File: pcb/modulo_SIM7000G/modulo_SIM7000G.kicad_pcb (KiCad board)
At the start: 2 copper layers, 100 x 50 mm, 56 parts, among them J1 Conn_01x04, J2 115Q-BCA0, J3 CONECTOR SERIAL, J4 Conn_01x02, J5 DCJ200-10-A-XX-X_REVA, Q1 NTE4153NT1G, Q2 NTE4153NT1G, Q3 NTE4153NT1G, U1 SIM7000G, U2 SN74LV1T34DCKR, U3 SN74LV1T34DCKR, U4 SN74LV1T34DCKR, U5 SN74LV1T34DCKR, U6 SN74LV1T34DCKR, U7 MIC29302WU, U8 LM1117-3.3

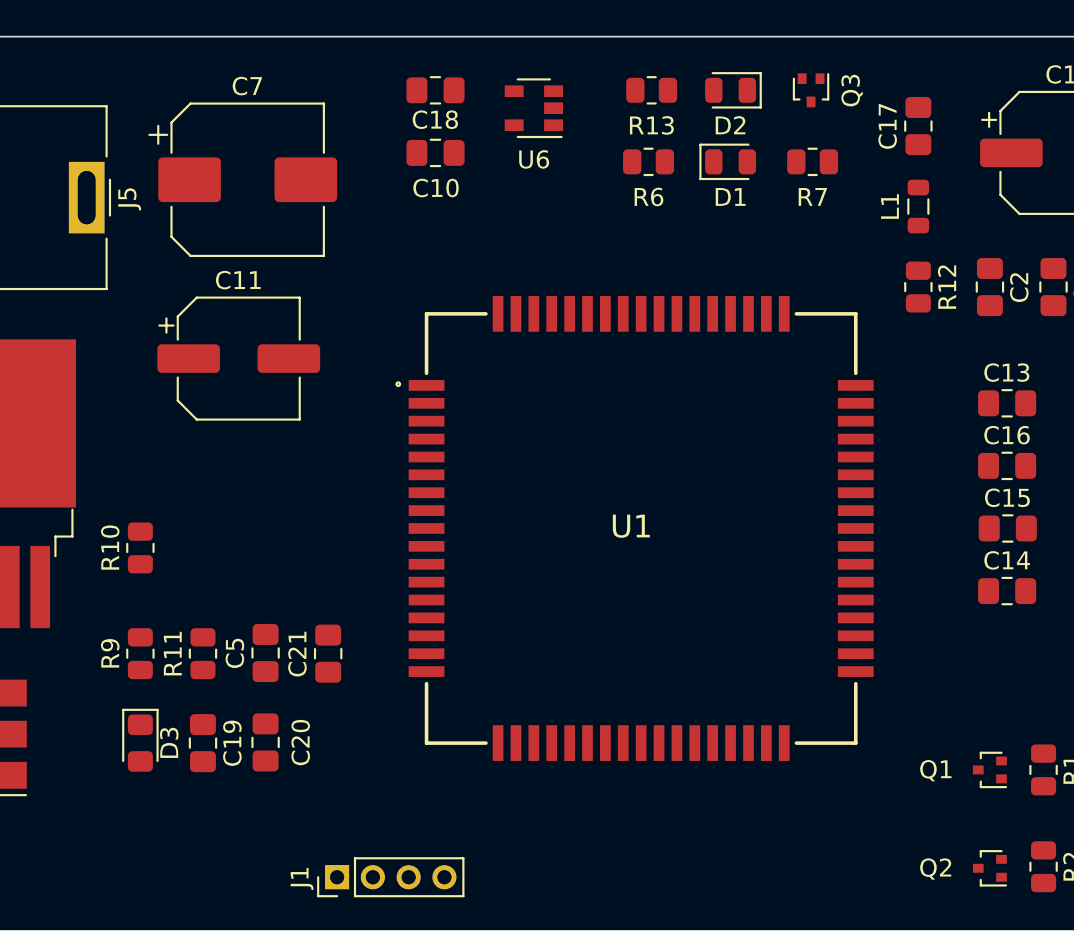
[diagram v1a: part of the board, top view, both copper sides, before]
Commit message: Se agrego connectores de antenas
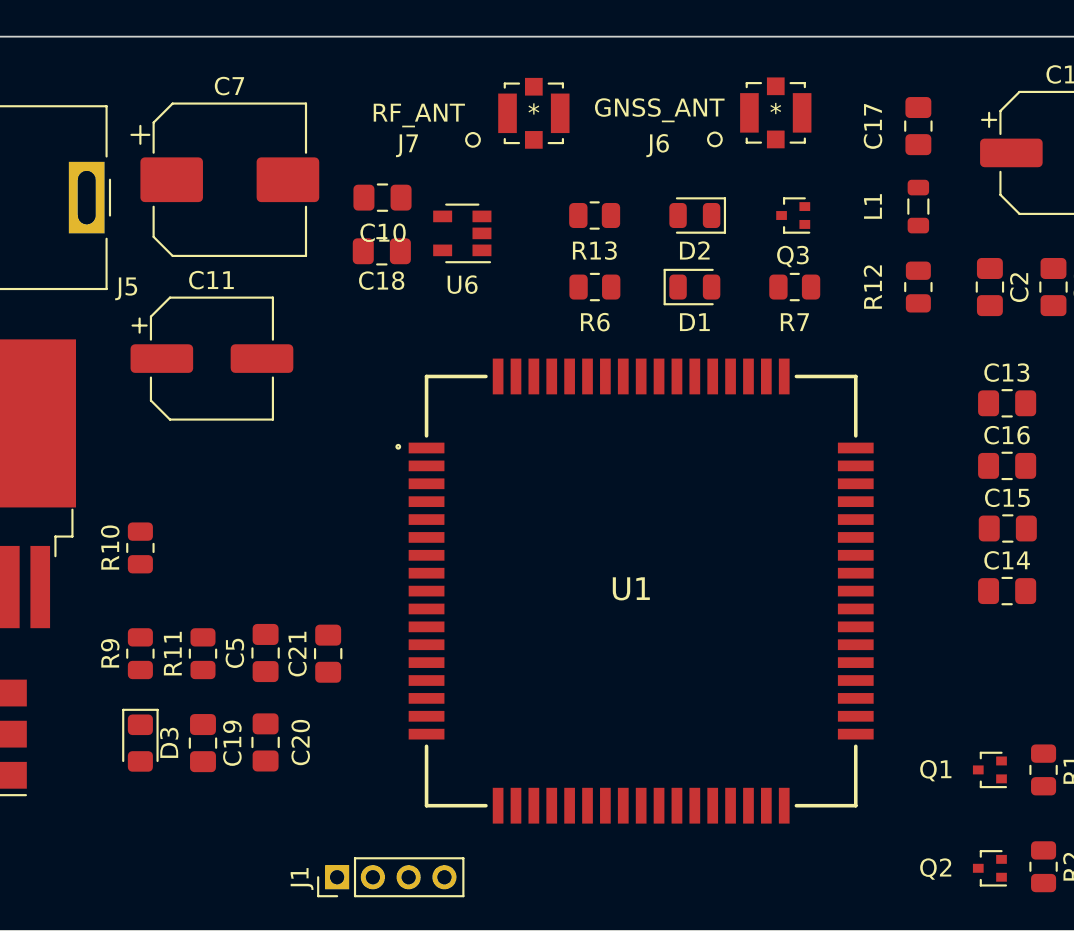
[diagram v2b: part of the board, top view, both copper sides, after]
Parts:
- added J6: GNSS_ANT, conn_ufl:1661, F.Cu at (148.5, 79.3)
- added J7: RF_ANT, conn_ufl:1661, F.Cu at (135.0, 79.3)
- moved C18 9.49 mm to (126.5, 87.0)
- moved U6 8.06 mm to (131.0, 86.0)
- moved R13 7.69 mm to (138.4, 85.0)
- moved R6 7.62 mm to (138.4, 89.0)
- moved D1 7.28 mm to (144.0, 89.0)
- moved D2 7.28 mm to (144.0, 85.0)
- moved Q3 7.07 mm to (149.5, 85.0), turned to 180 degrees
- moved R7 7.07 mm to (149.6, 89.0)
- moved C10 3.88 mm to (126.5, 84.0)
- moved U1 3.50 mm to (141.0, 106.0)
- moved C11 1.50 mm to (117.0, 93.0)
- moved C7 1.00 mm to (118.0, 83.0)
- turned C17 to 270 degrees

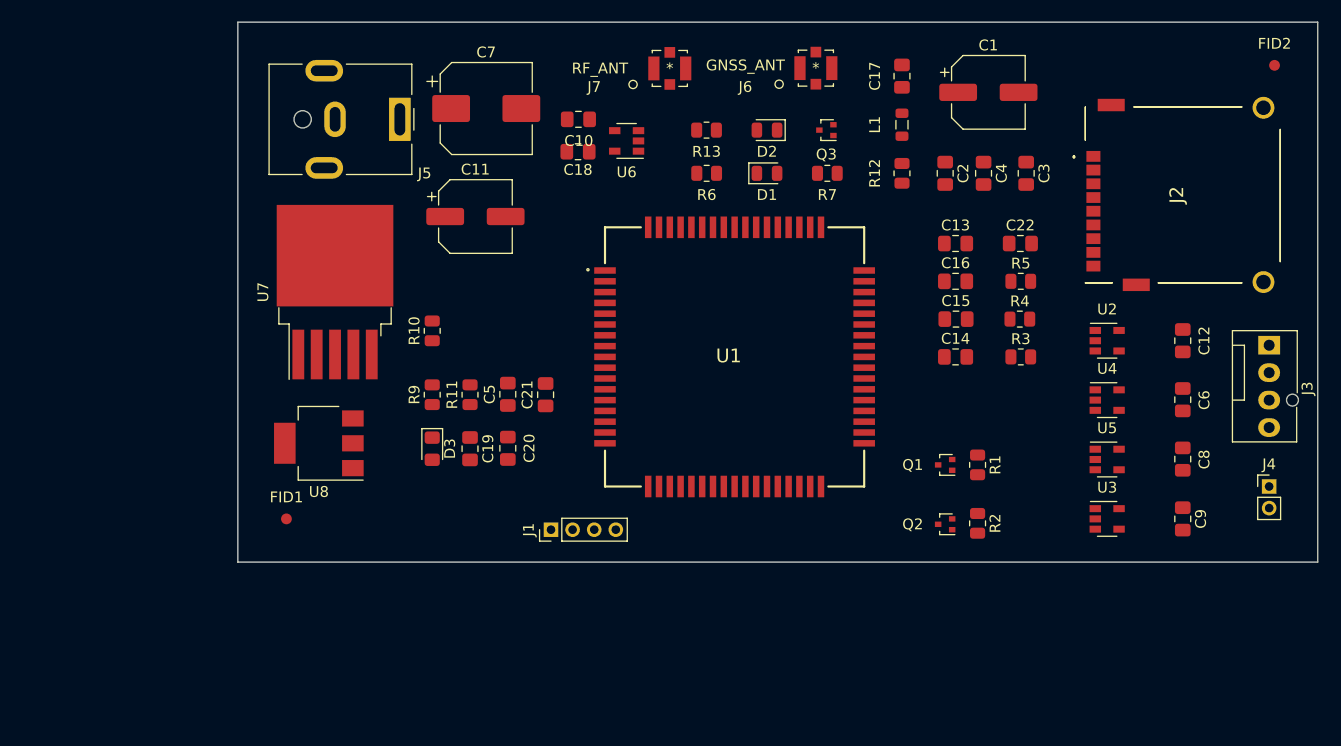
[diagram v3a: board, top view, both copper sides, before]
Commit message: correciones en el esquematico, se agrego agujeros de montaje
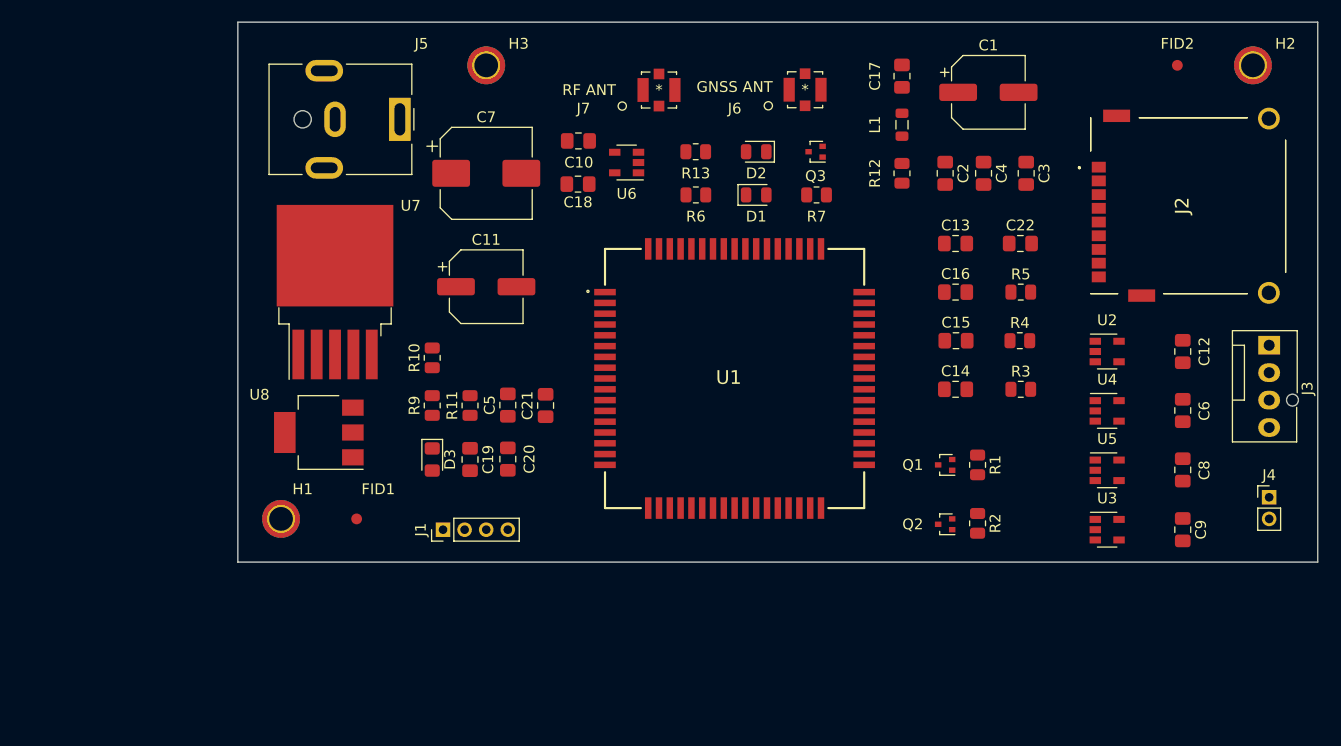
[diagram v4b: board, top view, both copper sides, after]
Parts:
- added H1: MountingHole, MountingHole:MountingHole_2.2mm_M2_ISO7380_Pad_TopBottom, F.Cu at (99.0, 121.0)
- added H2: MountingHole, MountingHole:MountingHole_2.2mm_M2_ISO7380_Pad_TopBottom, F.Cu at (189.0, 79.0)
- added H3: MountingHole, MountingHole:MountingHole_2.2mm_M2_ISO7380_Pad_TopBottom, F.Cu at (118.0, 79.0)
- J3: value CONECTOR SERIAL -> INTERFAZ SERIAL
- J5: value DCJ200-10-A-XX-X_REVA -> Jack-DC
- J6: value GNSS_ANT -> GNSS ANT
- J7: value RF_ANT -> RF ANT
- moved J1 10.0 mm to (114.0, 122.0)
- moved FID2 9.00 mm to (182.0, 79.0)
- moved C11 6.58 mm to (118.0, 99.5)
- moved FID1 6.50 mm to (106.0, 121.0)
- moved C7 6.00 mm to (118.0, 89.0)
- moved C14 3.00 mm to (161.5, 109.0)
- moved C18 3.00 mm to (126.5, 90.0)
- moved R3 3.00 mm to (167.5, 109.0)
- moved R10 2.50 mm to (113.0, 106.1)
- moved D1 2.24 mm to (143.0, 91.0)
- moved D2 2.24 mm to (143.0, 87.0)
- moved J6 2.24 mm to (147.5, 81.3)
- moved J7 2.24 mm to (134.0, 81.3)
- moved Q3 2.24 mm to (148.5, 87.0)
- moved R13 2.24 mm to (137.4, 87.0)
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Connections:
- net /+5VEXT renamed +5VD
- net /USB33 renamed +3V3
- net /VBAT renamed +BATT
- net /VDDX renamed VDD

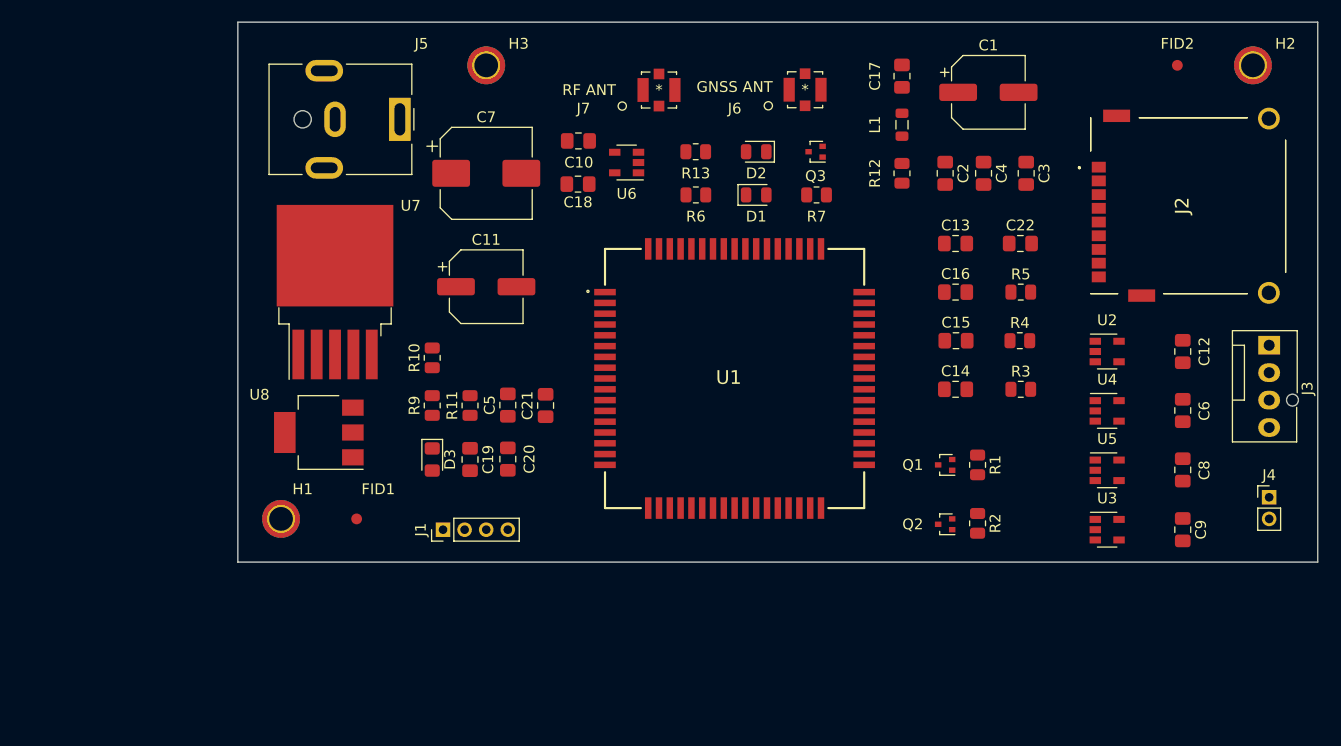
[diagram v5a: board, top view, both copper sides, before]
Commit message: se termino de diseñar las pistas. Falta plano de alimentacion y detalles
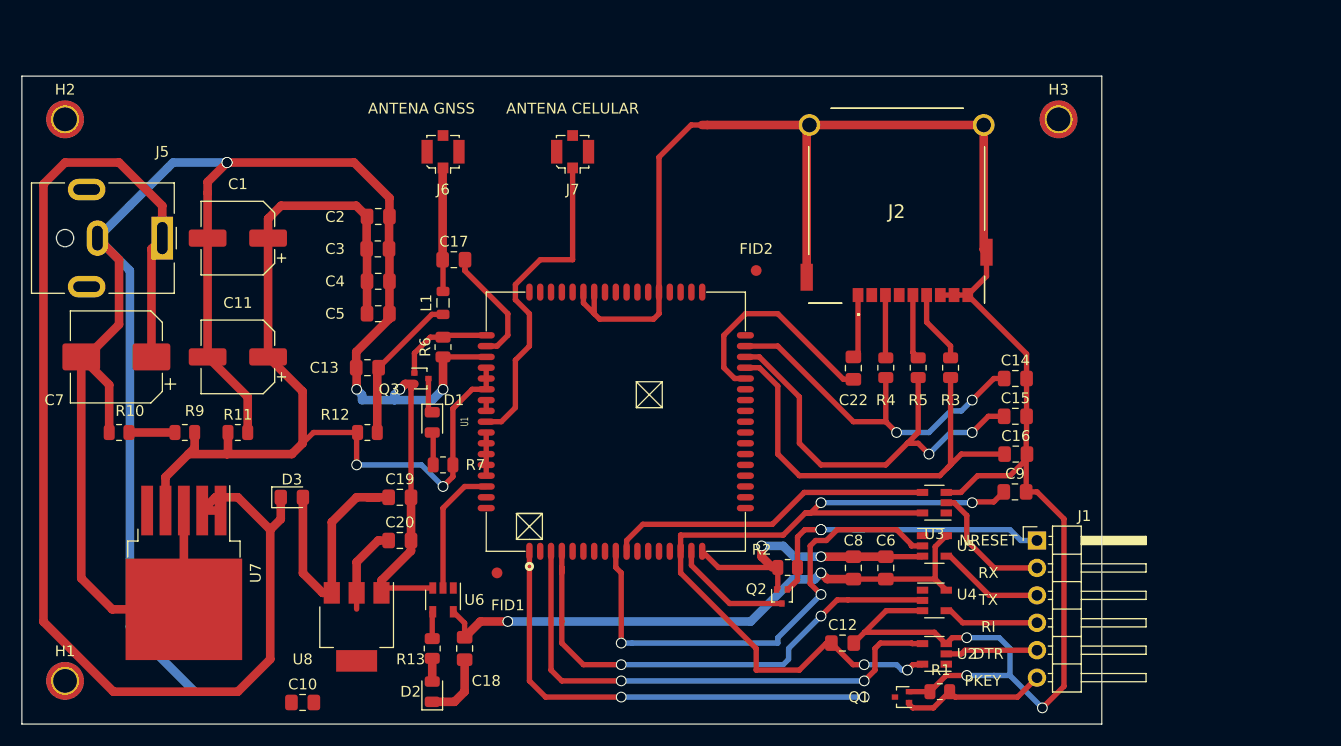
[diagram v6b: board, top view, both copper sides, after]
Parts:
- removed C21: 100nF, Capacitor_SMD:C_0805_2012Metric_Pad1.18x1.45mm_HandSolder
- removed J3: INTERFAZ SERIAL, Connector:FanPinHeader_1x04_P2.54mm_Vertical
- removed J4: Conn_01x02, Connector_PinHeader_2.00mm:PinHeader_1x02_P2.00mm_Vertical
- J1: value Conn_01x04 -> Conector Serial; footprint Connector_PinHeader_2.00mm:PinHeader_1x04_P2.00mm_Vertical -> Connector_PinHeader_2.54mm:PinHeader_1x06_P2.54mm_Horizontal
- J6: value GNSS ANT -> 1661; footprint conn_ufl:1661 -> Connector_Coaxial:U.FL_Molex_MCRF_73412-0110_Vertical
- J7: value RF ANT -> 1661; footprint conn_ufl:1661 -> Connector_Coaxial:U.FL_Molex_MCRF_73412-0110_Vertical
- U1: footprint RF_GSM:SIM7000 -> SIM7000G:SIM7000
- moved H2 110.1 mm to (79.0, 84.0)
- moved C1 70.8 mm to (95.0, 95.0), turned to 180 degrees
- moved C3 60.4 mm to (108.0, 96.0), turned to 0 degrees
- moved D2 58.3 mm to (113.0, 137.0), turned to 90 degrees
- moved C10 57.9 mm to (101.0, 138.0)
- moved C4 56.9 mm to (108.0, 99.0), turned to 0 degrees
- moved C13 55.7 mm to (107.0, 107.0), turned to 180 degrees
- moved R12 55.0 mm to (107.0, 113.0), turned to 0 degrees
- moved J1 55.0 mm to (169.0, 123.0), turned to 0 degrees
- moved H3 53.2 mm to (171.0, 84.0)
- moved C2 52.7 mm to (108.0, 93.0), turned to 0 degrees
- moved R13 52.1 mm to (113.0, 133.0), turned to 90 degrees
- moved L1 45.6 mm to (114.0, 101.0)
- moved C17 44.8 mm to (115.0, 97.0), turned to 0 degrees
- moved C18 44.3 mm to (116.0, 133.0), turned to 270 degrees
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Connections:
- J1 pad 1: Net-(C21-Pad1) -> /NRESET
- J1 pad 2: Net-(J1-Pad2) -> /RX
- J1 pad 3: Net-(J1-Pad3) -> /TX
- J1 pad 4: GND -> /RI
- J2 pad P1: Net-(C22-Pad2) -> Net-(C22-Pad1)
- Q1 pad 1: Net-(J4-Pad1) -> /POWERKEY
- Q2 pad 1: Net-(J4-Pad2) -> /NRESET
- R1 pad 2: Net-(J4-Pad1) -> /POWERKEY
- R2 pad 2: Net-(J4-Pad2) -> /NRESET
- R3 pad 1: Net-(C14-Pad1) -> Net-(J2-PadP7)
- R3 pad 2: Net-(J2-PadP7) -> Net-(C16-Pad1)
- R4 pad 1: Net-(C15-Pad1) -> Net-(J2-PadP2)
- R4 pad 2: Net-(J2-PadP3) -> Net-(C14-Pad1)
- R5 pad 1: Net-(C16-Pad1) -> Net-(J2-PadP3)
- R5 pad 2: Net-(J2-PadP2) -> Net-(C15-Pad1)
- U1 pad 24: Net-(C21-Pad1) -> Net-(U1-Pad24)
- U1 pad 27: Net-(J1-Pad3) -> Net-(U1-Pad27)
- U1 pad 28: Net-(J1-Pad2) -> Net-(U1-Pad28)
- U1 pad 30: Net-(C22-Pad1) -> Net-(C22-Pad2)
- U1 pad 31: Net-(C14-Pad1) -> Net-(C16-Pad1)
- U1 pad 33: Net-(C16-Pad1) -> Net-(C14-Pad1)
- U2 pad 2: Net-(J3-Pad1) -> /DTR
- U3 pad 2: Net-(J3-Pad4) -> /RX
- U4 pad 4: Net-(J3-Pad2) -> /RI
- U5 pad 4: Net-(J3-Pad3) -> /TX
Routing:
- net GND: track 0.00 -> 450.5 mm, vias 0 -> 10
- net +5VD: track 0.00 -> 118.5 mm
- net +BATT: track 0.00 -> 94.3 mm, vias 0 -> 2
- net VDD: track 0.00 -> 76.7 mm, vias 0 -> 4
- net +3V3: track 0.00 -> 63.5 mm, vias 0 -> 2
- net Net-(U1-Pad3): track 0.00 -> 48.5 mm, vias 0 -> 2
- net Net-(U1-Pad4): track 0.00 -> 46.3 mm, vias 0 -> 2
- net Net-(U1-Pad9): track 0.00 -> 46.0 mm, vias 0 -> 2
- net Net-(Q1-Pad3): track 0.00 -> 43.6 mm, vias 0 -> 2
- net Net-(C16-Pad1): track 0.00 -> 41.1 mm
- net Net-(C15-Pad1): track 0.00 -> 39.9 mm, vias 0 -> 2
- net Net-(C14-Pad1): track 0.00 -> 33.4 mm, vias 0 -> 2
- net Net-(J7-Pad1): track 0.00 -> 30.5 mm
- net Net-(U1-Pad10): track 0.00 -> 30.2 mm
- net /NRESET: track 0.00 -> 29.2 mm, vias 0 -> 2
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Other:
- board size 100 x 50 mm -> 100 x 60 mm
- board text added: "ANTENA CELULAR"
- board text added: "ANTENA GNSS"
- board text added: "DTR"
- board text added: "LECTOR SIM"
- board text added: "NRESET"
- board text added: "PKEY"
- board text added: "RI"
- board text added: "RX"
- board text added: "TX"
